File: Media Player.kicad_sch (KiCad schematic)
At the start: 74 parts, among them J1 PH2.0, J2 MEM2075-00-140-01-A, J3 USB_C_Receptacle_USB2.0_14P, J4 UART, Q2 DMP3068L-7, Q3 DMP3068L-7, SW1 BOOT, SW2 RESET, SW3 SW_Push, SW4 SW_Push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

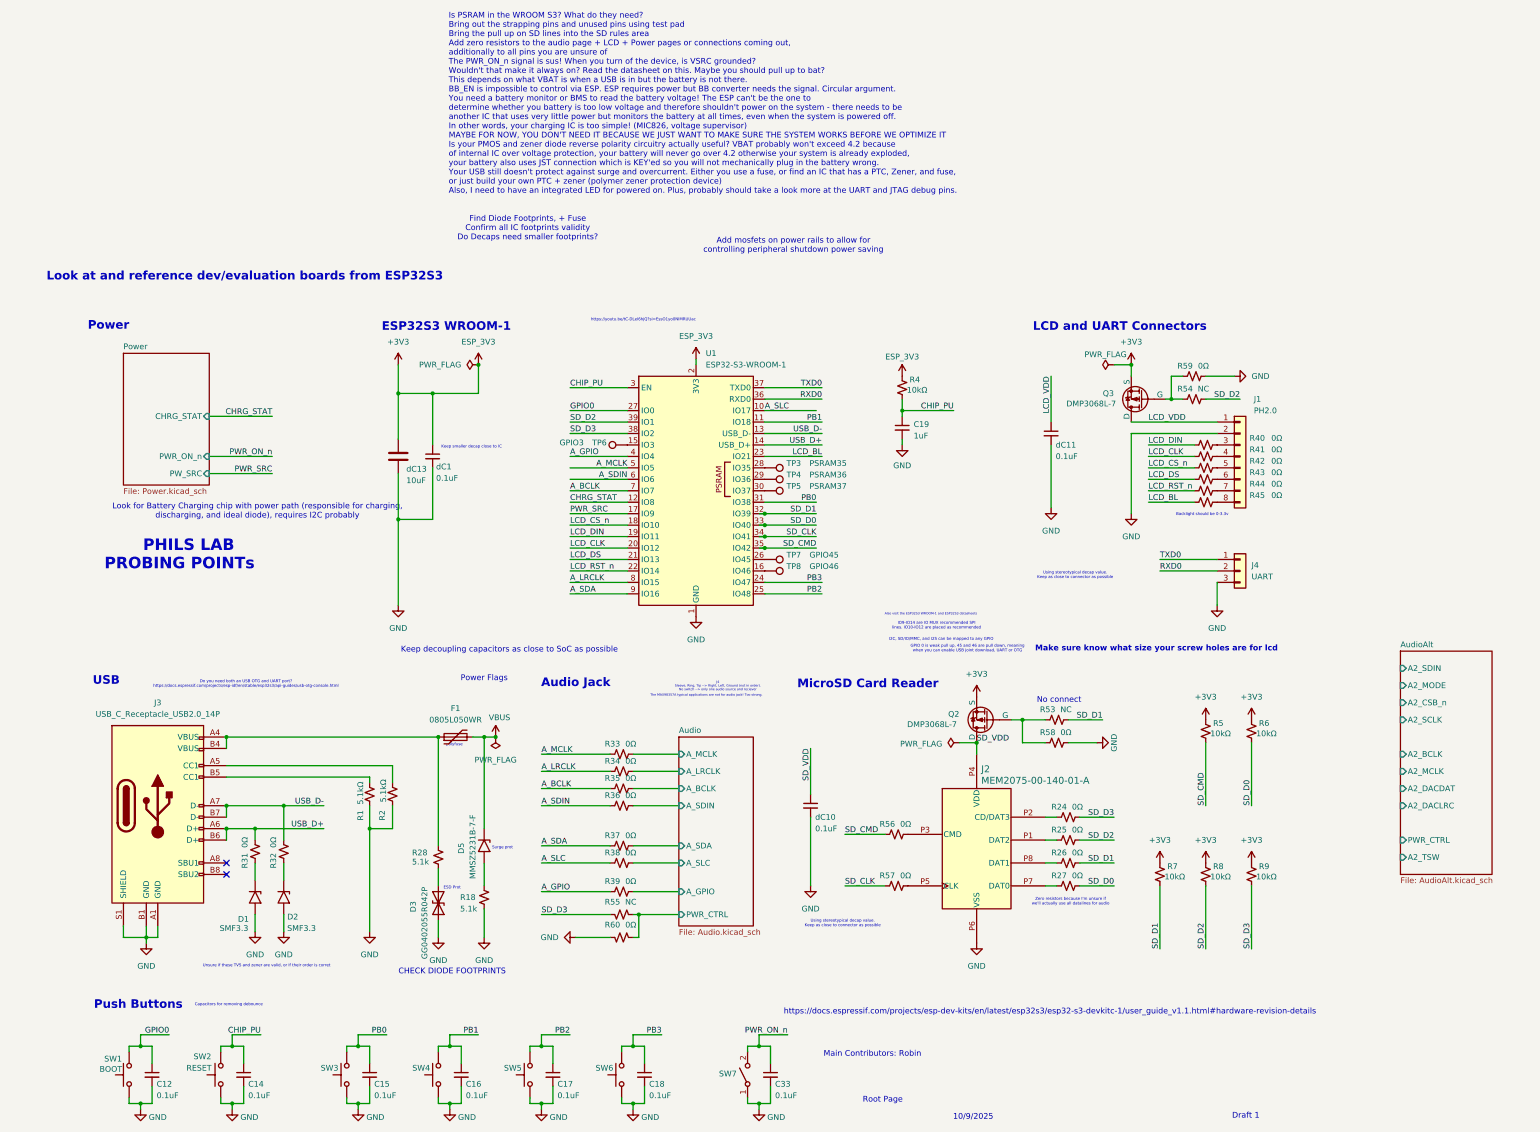
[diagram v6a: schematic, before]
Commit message: Board stuffing, new audio on board
Added new Audio IC to PCB.
Started moving everything into a estimated board size, AKA restricted area. Things seem REALL TIGHT. There's not enough space, I think I'll have to change resistor footprints
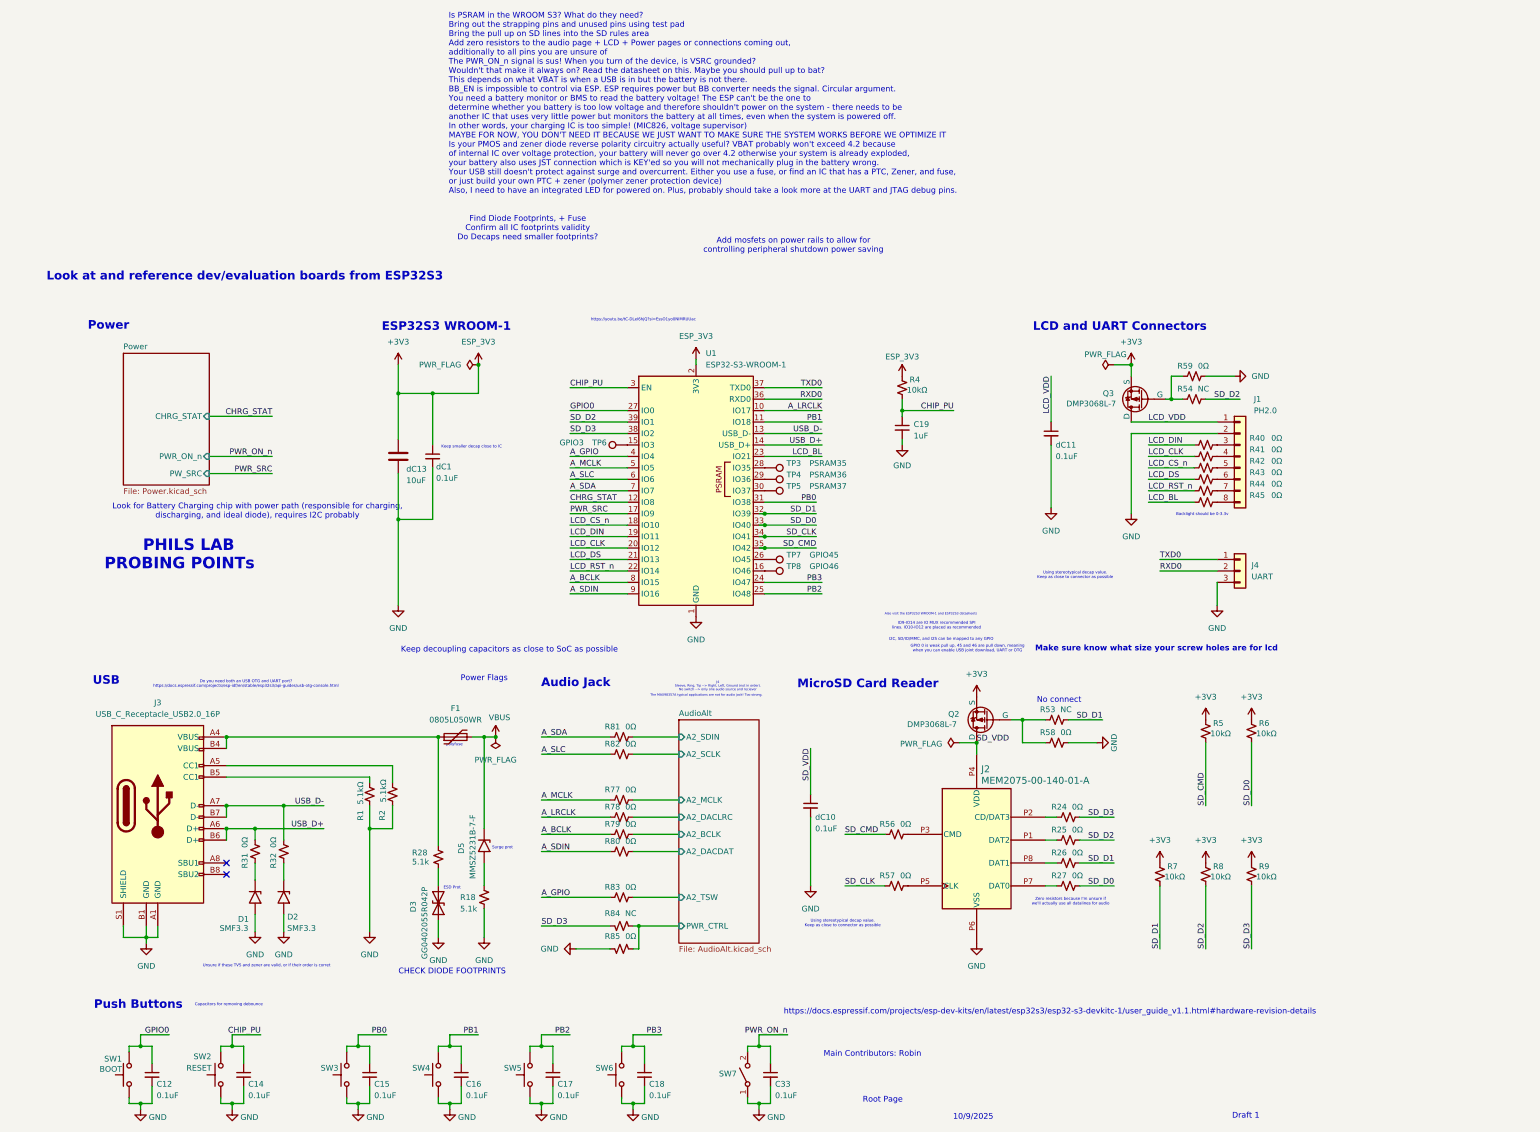
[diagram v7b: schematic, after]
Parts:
- removed R33, R34, R35, R36, R37, R38, R39, R60: 0Ω, Resistor_SMD:R_0805_2012Metric, symbol Device:R_Small_US
- removed R55: NC, Resistor_SMD:R_0805_2012Metric, symbol Device:R_Small_US
- added R77, R78, R79, R80, R81, R82, R83, R85: 0Ω, Resistor_SMD:R_0805_2012Metric, symbol Device:R_Small_US
- added R84: NC, Resistor_SMD:R_0805_2012Metric, symbol Device:R_Small_US
- J3: value USB_C_Receptacle_USB2.0_14P -> USB_C_Receptacle_USB2.0_16P
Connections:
- net A_BCLK: now also U1.8 (IO15), R79.1; no longer U1.7 (IO7)
- net A_GPIO: now also R83.1
- net A_LRCLK: now also U1.10 (IO17), R78.1; no longer U1.8 (IO15)
- net A_MCLK: now also R77.1
- net A_SDA: now also U1.7 (IO7), R81.1; no longer U1.9 (IO16)
- net A_SDIN: now also U1.9 (IO16), R80.1; no longer U1.6 (IO6)
- net A_SLC: now also U1.6 (IO6), R82.1; no longer U1.10 (IO17)
- net AudioAlt/A2_BCLK: now also R79.2
- net AudioAlt/A2_DACDAT: now also R80.2
- net AudioAlt/A2_DACLRC: now also R78.2
- net AudioAlt/A2_MCLK: now also R77.2
- net AudioAlt/A2_SCLK: now also R82.2
- net AudioAlt/A2_SDIN: now also R81.2
- net AudioAlt/A2_TSW: now also R83.2
- net AudioAlt/PWR_CTRL: now also R84.1, R85.1
- net GND: now also R85.2
- net SD_D3: now also R84.2
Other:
- removed sheet Audio
- sheet AudioAlt ports: added none; removed A2_CSB_n, A2_MODE

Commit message: Draft 1
I'm not very fond of some of my traces. Especially the power component. Not even sure if all components are routed properly. Still missing GND and PWR plane, so most component power not routed. Missing LCD screw holes. Power and signal traces are using same width/thickness, and also have not checked with what JLC allows during fabrication. I should try again, working from general (blocking) to specifics (details), much like how I started with schematics. Many conventions I have not learned.
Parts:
- R77, R78, R79, R80, R81, R82, R83, R84, R85: footprint Resistor_SMD:R_0805_2012Metric -> Resistor_SMD:R_0603_1608Metric_Pad0.98x0.95mm_HandSolder
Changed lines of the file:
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@@
 			)
 		)
-		(property "Footprint" "Resistor_SMD:R_0805_2012Metric"
+		(property "Footprint" "Resistor_SMD:R_0603_1608Metric_Pad0.98x0.95mm_HandSolder"
 			(at 134.62 127 0)
 			(effects
@@
 			)
 		)
-		(property "Footprint" "Resistor_SMD:R_0805_2012Metric"
+		(property "Footprint" "Resistor_SMD:R_0603_1608Metric_Pad0.98x0.95mm_HandSolder"
 			(at 134.62 109.22 0)
 			(effects
@@
 			)
 		)
-		(property "Footprint" "Resistor_SMD:R_0805_2012Metric"
+		(property "Footprint" "Resistor_SMD:R_0603_1608Metric_Pad0.98x0.95mm_HandSolder"
 			(at 134.62 130.81 0)
 			(effects
@@
 			)
 		)
-		(property "Footprint" "Resistor_SMD:R_0805_2012Metric"
+		(property "Footprint" "Resistor_SMD:R_0603_1608Metric_Pad0.98x0.95mm_HandSolder"
 			(at 134.62 156.21 0)
 			(effects
@@
 			)
 		)
-		(property "Footprint" "Resistor_SMD:R_0805_2012Metric"
+		(property "Footprint" "Resistor_SMD:R_0603_1608Metric_Pad0.98x0.95mm_HandSolder"
 			(at 134.62 134.62 0)
 			(effects
@@
 			)
 		)
-		(property "Footprint" "Resistor_SMD:R_0805_2012Metric"
+		(property "Footprint" "Resistor_SMD:R_0603_1608Metric_Pad0.98x0.95mm_HandSolder"
 			(at 134.62 151.13 0)
 			(effects
@@
 			)
 		)
-		(property "Footprint" "Resistor_SMD:R_0805_2012Metric"
+		(property "Footprint" "Resistor_SMD:R_0603_1608Metric_Pad0.98x0.95mm_HandSolder"
 			(at 134.62 113.03 0)
 			(effects
@@
 			)
 		)
-		(property "Footprint" "Resistor_SMD:R_0805_2012Metric"
+		(property "Footprint" "Resistor_SMD:R_0603_1608Metric_Pad0.98x0.95mm_HandSolder"
 			(at 134.62 144.78 0)
 			(effects
@@
 			)
 		)
-		(property "Footprint" "Resistor_SMD:R_0805_2012Metric"
+		(property "Footprint" "Resistor_SMD:R_0603_1608Metric_Pad0.98x0.95mm_HandSolder"
 			(at 134.62 123.19 0)
 			(effects
